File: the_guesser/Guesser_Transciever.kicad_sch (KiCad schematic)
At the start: 51 parts, among them J2 Conn_Coaxial, J3 BMI-S-209-F, U3 CC1101RGPR, U4 CC1190RGVR, U5 B39921B3728U410, X1 STDCRG2-27M

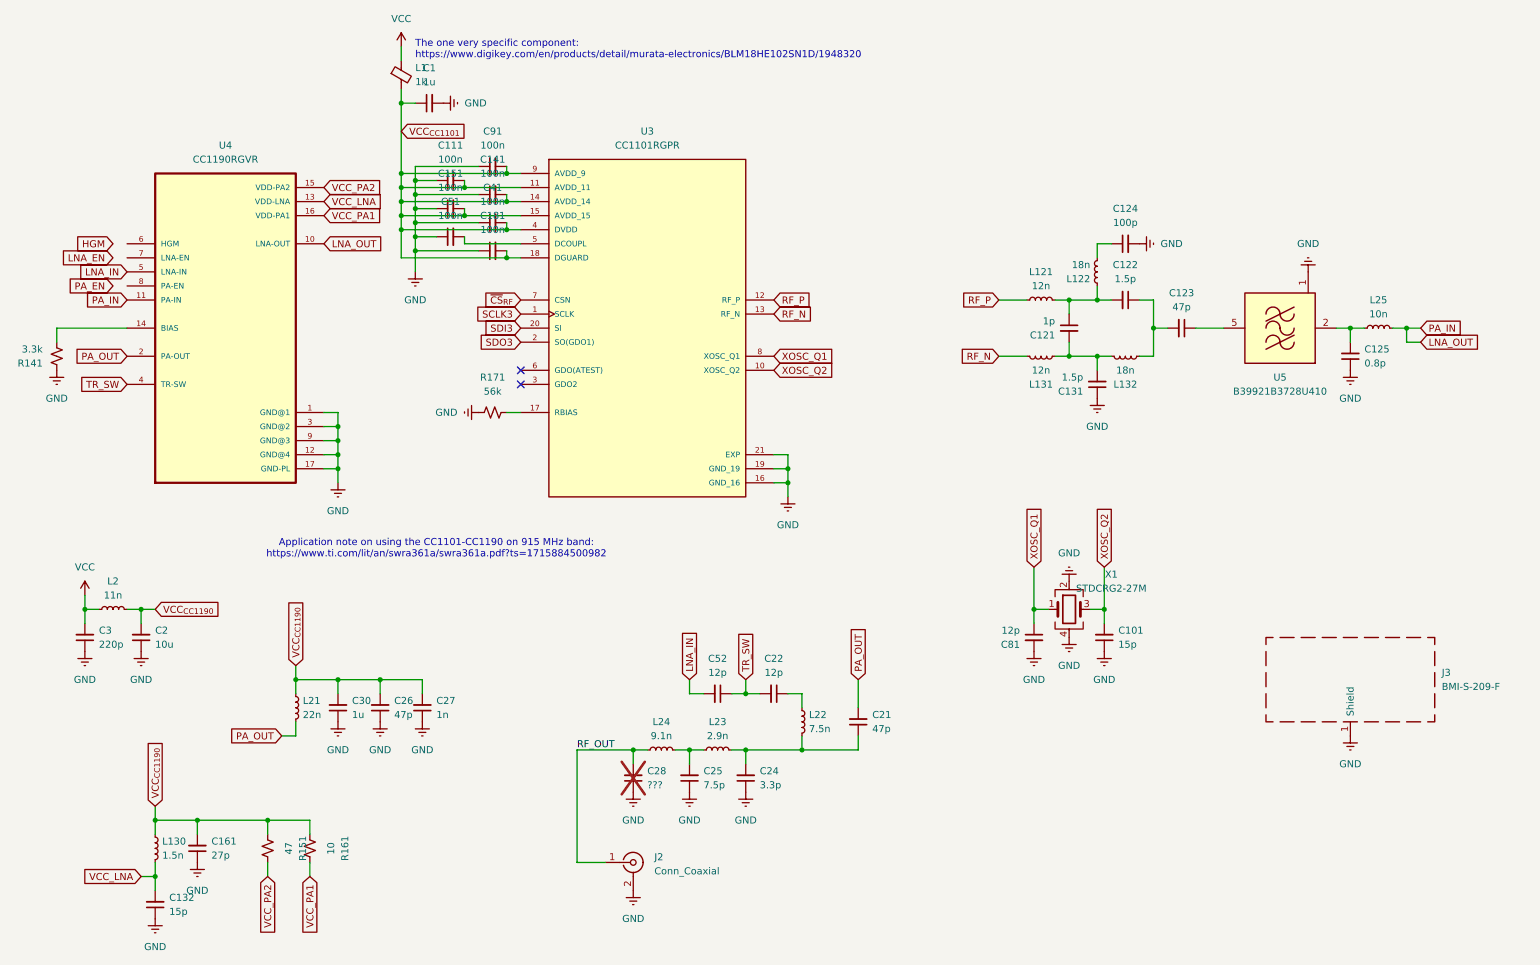
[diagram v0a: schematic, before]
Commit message: Updated Guesser USB and GPS
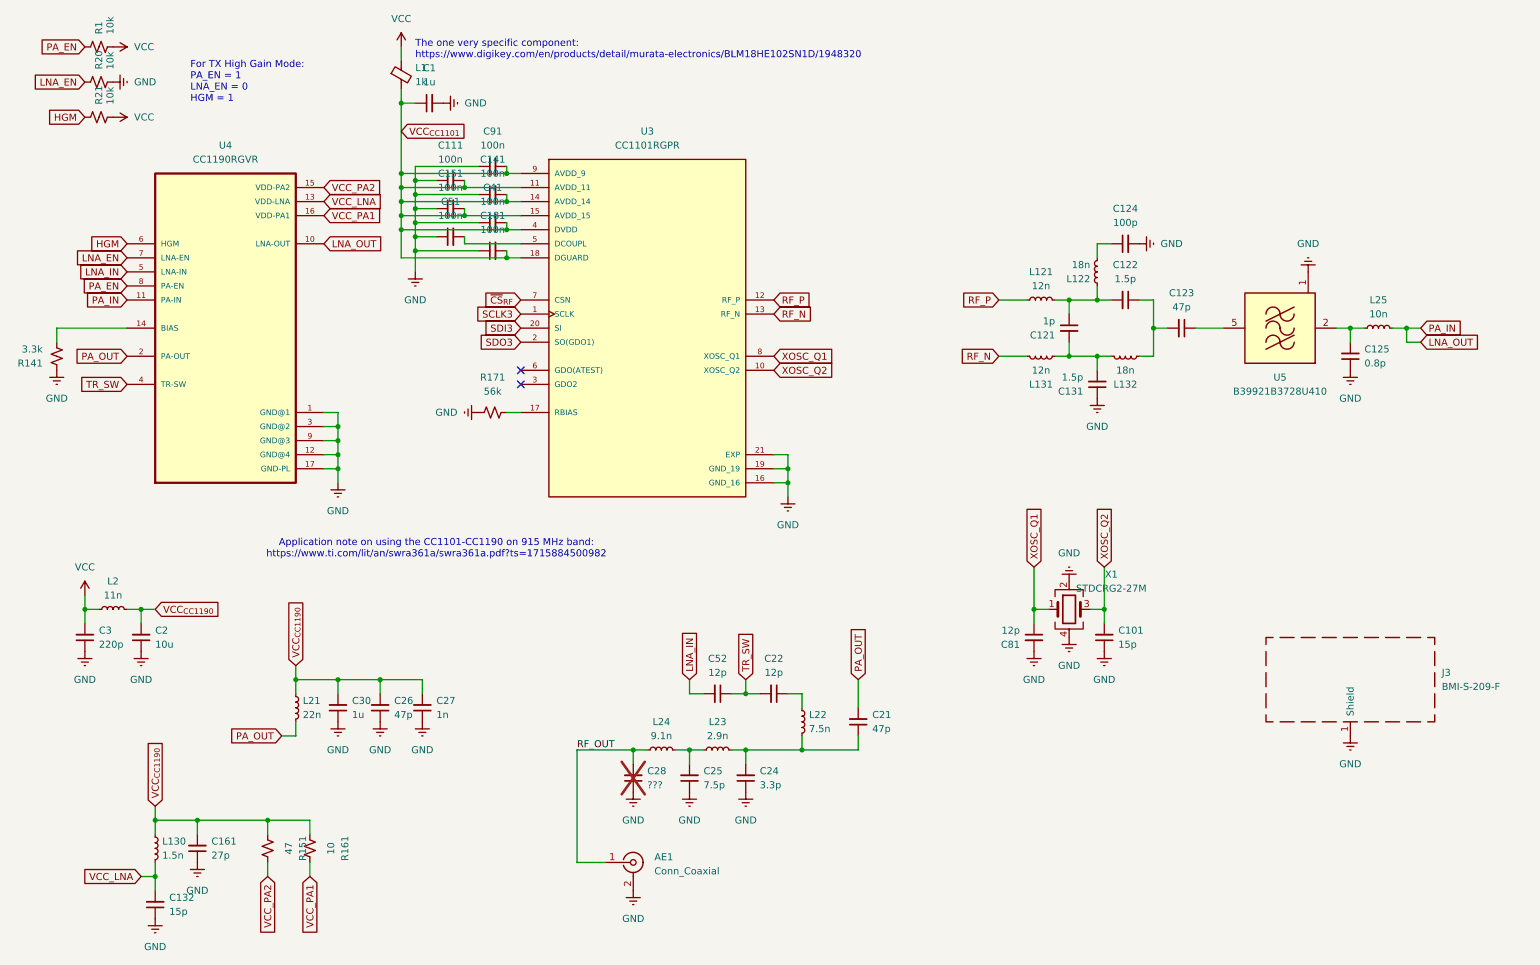
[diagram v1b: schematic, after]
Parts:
- added R1, R20, R21: 10k, Resistor_SMD:R_0603_1608Metric, symbol Device:R_Small_US
- renumbered J2 to AE1
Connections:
- net GND: now also R20.2
- net HGM: now also U4.6 (HGM), R21.1
- net LNA_EN: now also U4.7 (LNA-EN), R20.1
- net PA_EN: now also U4.8 (PA-EN), R1.1
- net VCC: now also R1.2, R21.2
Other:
- note added: "For TX High Gain Mode: PA_EN = 1 LNA_EN = 0 HGM = 1"
